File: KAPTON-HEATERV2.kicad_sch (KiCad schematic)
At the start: 26 parts, among them J1 XT60PW-M, J2 XT60PW-M, J3 1985276, J4 1985218, J5 10090926-P154XLF, K1 1-1393210-8, Q1 AO3400A, U1 TC4427ACOA, U2 INA181

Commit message: need to finish netclasses
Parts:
- added D3: SMCJ30CA, PCM_JLCPCB:D_SMC, symbol PCM_JLCPCB-Diodes:TVS-Bi,SMCJ30CA
- added R8: R27, symbol Device:R
- C4: value C19nf -> C4.7nf; footprint Capacitor_SMD:C_0805_2012Metric -> (none)
- MOSFET1: value SIR462DP-T1-GE3 -> SIR626ADP
- R6: value R10 -> R5
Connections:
- net GND: now also D3.2
- net HEATER OUT: now also D3.1, R8.2
- net at K1.3: now also F1.2
- net at MOSFET1.4, R6.1: no longer C4.1
- net 24VIN: no longer names the net of F1.1, J2.2 (Pin_2)
- new net: C4.1, R8.1
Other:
- moved on the sheet: F1, J2, R6

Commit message: iteration 1.2
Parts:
- C4: footprint (none) -> Capacitor_SMD:C_0805_2012Metric
- R8: footprint (none) -> Resistor_SMD:R_1206_3216Metric
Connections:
- net 24V: now also D2.3 (K)
- net HEATER OUT: now also MOSFET1.9
- no-connect marks 6 -> 7
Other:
- moved on the sheet: R5
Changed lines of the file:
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@@
 	)
 	(junction
-		(at 266.7 111.76)
-		(diameter 0)
-		(color 0 0 0 0)
-	)
-	(junction
 		(at 201.93 129.54)
 		(diameter 0)
@@
 	)
 	(junction
-		(at 266.7 109.22)
+		(at 69.85 53.34)
 		(diameter 0)
 		(color 0 0 0 0)
 	)
 	(junction
-		(at 266.7 106.68)
+		(at 111.76 77.47)
 		(diameter 0)
 		(color 0 0 0 0)
 	)
 	(junction
-		(at 69.85 53.34)
+		(at 226.06 106.68)
 		(diameter 0)
 		(color 0 0 0 0)
 	)
 	(junction
-		(at 111.76 77.47)
+		(at 266.7 111.76)
 		(diameter 0)
 		(color 0 0 0 0)
 	)
 	(junction
-		(at 226.06 106.68)
+		(at 113.03 107.95)
 		(diameter 0)
 		(color 0 0 0 0)
 	)
 	(junction
-		(at 113.03 107.95)
+		(at 100.33 107.95)
 		(diameter 0)
 		(color 0 0 0 0)
 	)
 	(junction
-		(at 100.33 107.95)
+		(at 266.7 109.22)
 		(diameter 0)
 		(color 0 0 0 0)
@@
 	)
 	(junction
+		(at 266.7 106.68)
+		(diameter 0)
+		(color 0 0 0 0)
+	)
+	(junction
 		(at 99.06 146.05)
 		(diameter 0)
@@
 		(at 88.9 110.49)
 	)
+	(no_connect
+		(at 50.8 102.87)
+	)
 	(wire
 		(pts
@@
 	(wire
 		(pts
+			(xy 93.98 146.05) (xy 99.06 146.05)
+		)
+		(stroke
+			(width 0)
+			(type default)
+		)
+	)
+	(wire
+		(pts
 			(xy 27.94 102.87) (xy 29.21 102.87)
 		)
@@
 	(wire
 		(pts
-			(xy 125.73 53.34) (xy 133.35 53.34)
+			(xy 266.7 106.68) (xy 266.7 109.22)
 		)
 		(stroke
@@
 	(wire
 		(pts
-			(xy 111.76 60.96) (xy 111.76 62.23)
+			(xy 125.73 53.34) (xy 133.35 53.34)
 		)
 		(stroke
@@
 	(wire
 		(pts
-			(xy 38.1 102.87) (xy 46.99 102.87)
+			(xy 111.76 60.96) (xy 111.76 62.23)
 		)
 		(stroke
@@
 	(wire
 		(pts
-			(xy 46.99 107.95) (xy 50.8 107.95)
+			(xy 38.1 102.87) (xy 46.99 102.87)
 		)
 		(stroke
@@
 	(wire
 		(pts
-			(xy 113.03 107.95) (xy 100.33 107.95)
+			(xy 46.99 107.95) (xy 50.8 107.95)
 		)
 		(stroke
@@
 	(wire
 		(pts
-			(xy 266.7 111.76) (xy 266.7 114.3)
+			(xy 113.03 107.95) (xy 100.33 107.95)
 		)
 		(stroke
@@
 	(wire
 		(pts
-			(xy 93.98 146.05) (xy 99.06 146.05)
+			(xy 201.93 129.54) (xy 231.14 129.54)
 		)
 		(stroke
@@
 	(wire
 		(pts
-			(xy 201.93 129.54) (xy 231.14 129.54)
+			(xy 266.7 109.22) (xy 266.7 111.76)
 		)
 		(stroke
@@
 	(wire
 		(pts
-			(xy 266.7 109.22) (xy 266.7 111.76)
+			(xy 104.14 67.31) (xy 106.68 67.31)
 		)
 		(stroke
@@
 	(wire
 		(pts
-			(xy 266.7 106.68) (xy 266.7 109.22)
+			(xy 82.55 134.62) (xy 82.55 146.05)
 		)
 		(stroke
@@
 	(wire
 		(pts
-			(xy 82.55 134.62) (xy 82.55 146.05)
+			(xy 111.76 57.15) (xy 111.76 60.96)
 		)
 		(stroke
@@
 	(wire
 		(pts
-			(xy 111.76 57.15) (xy 111.76 60.96)
+			(xy 266.7 111.76) (xy 266.7 114.3)
 		)
 		(stroke
@@
 	(wire
 		(pts
+			(xy 104.14 72.39) (xy 106.68 72.39)
+		)
+		(stroke
+			(width 0)
+			(type default)
+		)
+	)
+	(wire
+		(pts
 			(xy 201.93 106.68) (xy 226.06 106.68)
 		)
@@
 	(global_label "SHUNT LOW"
 		(shape input)
-		(at 106.68 72.39 180)
+		(at 104.14 72.39 180)
 		(fields_autoplaced yes)
 		(effects
@@
 		)
 		(property "Intersheetrefs" "${INTERSHEET_REFS}"
-			(at 92.7486 72.39 0)
+			(at 90.2086 72.39 0)
 			(effects
 				(font
@@
 	(global_label "SHUNT HIGH"
 		(shape input)
-		(at 106.68 67.31 180)
+		(at 104.14 67.31 180)
 		(fields_autoplaced yes)
 		(effects
@@
 		)
 		(property "Intersheetrefs" "${INTERSHEET_REFS}"
-			(at 92.0228 67.31 0)
+			(at 89.4828 67.31 0)
 			(effects
 				(font
@@
 		)
 	)
+	(netclass_flag ""
+		(length 2.54)
+		(shape round)
+		(at 39.37 80.01 180)
+		(fields_autoplaced yes)
+		(effects
+			(font
+				(size 1.27 1.27)
+			)
+			(justify right bottom)
+		)
+		(property "Netclass" "24V"
+			(at 40.0685 82.55 0)
+			(effects
+				(font
+					(size 1.27 1.27)
+				)
+				(justify left)
+			)
+		)
+		(property "Component Class" ""
+			(at -194.31 -49.53 0)
+			(effects
+				(font
+					(size 1.27 1.27)
+					(italic yes)
+				)
+			)
+		)
+	)
+	(netclass_flag ""
+		(length 2.54)
+		(shape round)
+		(at 94.615 146.05 180)
+		(fields_autoplaced yes)
+		(effects
+			(font
+				(size 1.27 1.27)
+			)
+			(justify right bottom)
+		)
+		(property "Netclass" "24V"
+			(at 95.3135 148.59 0)
+			(effects
+				(font
+					(size 1.27 1.27)
+				)
+				(justify left)
+			)
+		)
+		(property "Component Class" ""
+			(at -139.065 16.51 0)
+			(effects
+				(font
+					(size 1.27 1.27)
+					(italic yes)
+				)
+			)
+		)
+	)
+	(netclass_flag ""
+		(length 2.54)
+		(shape round)
+		(at 105.41 67.31 0)
+		(fields_autoplaced yes)
+		(effects
+			(font
+				(size 1.27 1.27)
+			)
+			(justify left bottom)
+		)
+		(property "Netclass" "DEF2"
+			(at 106.1085 64.77 0)
+			(effects
+				(font
+					(size 1.27 1.27)
+				)
+				(justify left)
+				(hide yes)
+			)
+		)
+		(property "Component Class" ""
+			(at -59.69 3.81 0)
+			(effects
+				(font
+					(size 1.27 1.27)
+					(italic yes)
+				)
+			)
+		)
+	)
+	(netclass_flag ""
+		(length 2.54)
+		(shape round)
+		(at 82.55 137.16 90)
+		(fields_autoplaced yes)
+		(effects
+			(font
+				(size 1.27 1.27)
+			)
+			(justify left bottom)
+		)
+		(property "Netclass" "24V"
+			(at 80.01 136.4615 90)
+			(effects
+				(font
+					(size 1.27 1.27)
+				)
+				(justify left)
+			)
+		)
+		(property "Component Class" ""
+			(at -151.13 7.62 0)
+			(effects
+				(font
+					(size 1.27 1.27)
+					(italic yes)
+				)
+			)
+		)
+	)
+	(netclass_flag ""
+		(length 2.54)
+		(shape round)
+		(at 58.42 78.74 270)
+		(fields_autoplaced yes)
+		(effects
+			(font
+				(size 1.27 1.27)
+			)
+			(justify right bottom)
+		)
+		(property "Netclass" "24V"
+			(at 60.96 78.0415 90)
+			(effects
+				(font
+					(size 1.27 1.27)
+				)
+				(justify left)
+			)
+		)
+		(property "Component Class" ""
+			(at -175.26 -50.8 0)
+			(effects
+				(font
+					(size 1.27 1.27)
+					(italic yes)
+				)
+			)
+		)
+	)
+	(netclass_flag ""
+		(length 2.54)
+		(shape round)
+		(at 91.44 134.62 180)
+		(fields_autoplaced yes)
+		(effects
+			(font
+				(size 1.27 1.27)
+			)
+			(justify right bottom)
+		)
+		(property "Netclass" "24V"
+			(at 92.1385 137.16 0)
+			(effects
+				(font
+					(size 1.27 1.27)
+				)
+				(justify left)
+			)
+		)
+		(property "Component Class" ""
+			(at -142.24 5.08 0)
+			(effects
+				(font
+					(size 1.27 1.27)
+					(italic yes)
+				)
+			)
+		)
+	)
 	(symbol
 		(lib_id "power:GND")
@@
 			)
 		)
-		(property "Footprint" ""
+		(property "Footprint" "Resistor_SMD:R_1206_3216Metric"
 			(at 241.3 142.748 90)
 			(effects
@@
 		(pin "2"
 		)
+		(pin "3"
+		)
 		(pin "1"
 		)
@@
 		(on_board yes)
 		(dnp no)
-		(fields_autoplaced yes)
 		(property "Reference" "MOSFET1"
 			(at 246.38 96.52 0)
@@
 			)
 		)
-		(pin "8"
+		(pin "9"
 		)
 		(pin "6"
@@
 		(pin "4"
 		)
+		(pin "8"
+		)
 		(instances
 			(project "KAPTON-HEATERV2"
@@
 			)
 		)
-		(property "Footprint" ""
+		(property "Footprint" "Capacitor_SMD:C_0805_2012Metric"
 			(at 224.79 141.9352 0)
 			(effects
@@
 	(symbol
 		(lib_id "Device:R")
-		(at 99.06 140.97 180)
+		(at 99.06 140.97 0)
+		(mirror x)
 		(unit 1)
 		(exclude_from_sim no)
@@
 		(dnp no)
 		(property "Reference" "R5"
-			(at 105.156 142.24 0)
+			(at 92.964 142.24 0)
 			(effects
 				(font
@@
 		)
 		(property "Value" "R0.001"
-			(at 109.474 139.7 0)
+			(at 88.646 139.7 0)
 			(effects
 				(font
@@
 		)
 		(property "Footprint" "CRE2512_FZ_R001E_2 (1):RESC6432X90N"
-			(at 100.838 140.97 90)
+			(at 97.282 140.97 90)
 			(effects
 				(font

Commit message: June 26 New Traces
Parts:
- removed D2: V20DM100C-M3/I, Package_TO_SOT_SMD:TO-263-2, symbol Device:D
- removed J1, J2: XT60PW-M, XT60PW-M:AMASS_XT60PW-M, symbol Connector_Generic:Conn_01x02
- added C10, C7: C4.7uf, Capacitor_SMD:C_0805_2012Metric, symbol Device:C
- added C8, C9: C0.1uf, Capacitor_SMD:C_0805_2012Metric, symbol Device:C
- added D2: V20DM100C-M3_I, V40DL45BPM3I, symbol V20DM100C-M3_I:V20DM100C-M3_I
- added J1, J2: XT60PW-M, XT60PW-M:AMASS_XT60PW-M, symbol XT60PW-M:XT60PW-M
- C4: footprint Capacitor_SMD:C_0805_2012Metric -> KCM55LR71J475KH01K:CAPC6153X300N
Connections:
- net 24V: now also D2.3 (K), J1.1 (+)
- net 5V: now also C10.1, C7.1, C8.1, C9.1
- net GND: now also C10.2, C7.2, C8.2, C9.2, J2.1 (+)
- net HEATER OUT: now also D2.1 (A_1), D2.2 (A_2)
- net SHUNT HIGH: now also J1.2 (-)
- net at F1.1: now also J2.2 (-)
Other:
- moved on the sheet: R5

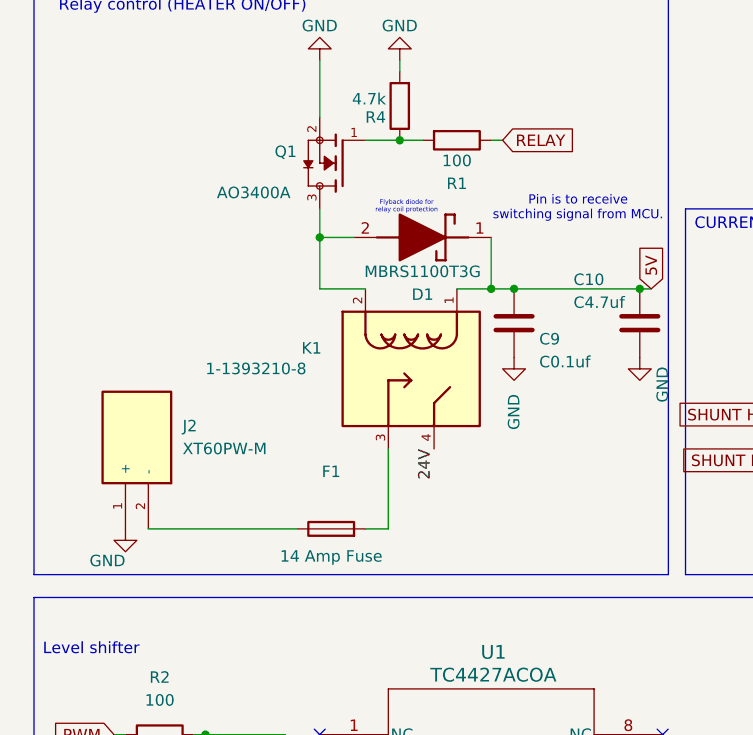
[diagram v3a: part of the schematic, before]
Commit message: New Relay Footprint
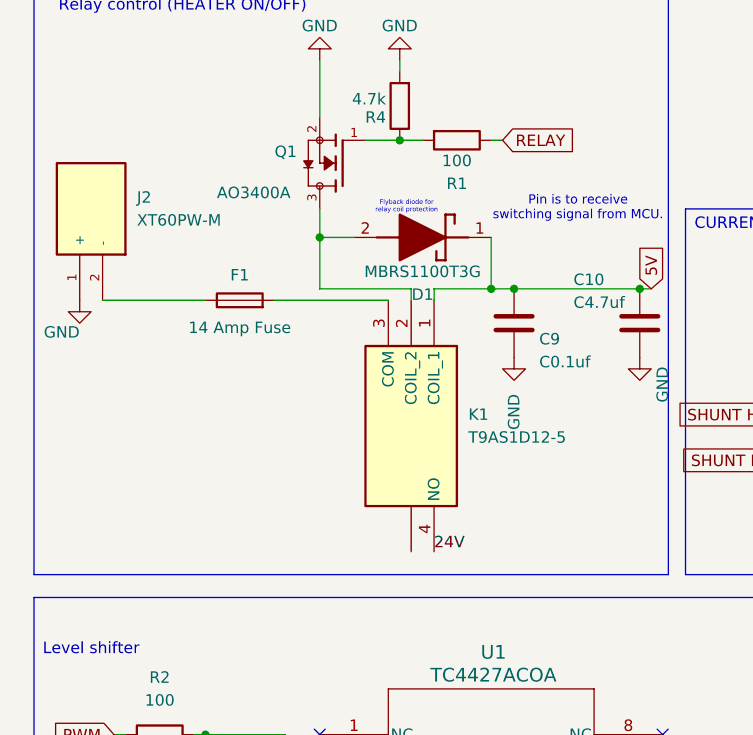
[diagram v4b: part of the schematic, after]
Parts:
- removed K1: 1-1393210-8, T9AS1D12_24:RELAY_1-1393210-8, symbol 1-1393210-8:1-1393210-8
- added K1: T9AS1D12-5, T9AS1D125, symbol T9AS1D12-5:T9AS1D12-5
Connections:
- net 24V: now also K1.4 (NO)
- net 5V: now also K1.1 (COIL_1)
- net at D1.2 (A), Q1.3: now also K1.2 (COIL_2)
- net at F1.2: now also K1.3 (COM)
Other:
- moved on the sheet: F1, J2
